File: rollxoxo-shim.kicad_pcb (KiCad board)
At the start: 4 copper layers, 70 parts, among them J1 USB_C_Receptacle_USB2.0_14P, J2 Conn_01x02, J3 Conn_01x10, J4 Conn_01x01, J5 Conn_01x10, J6 Conn_01x03, J7 Conn_01x01, SW1 SW_Push, SW2 SW_Push, U1 SN74LV1T125DBV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

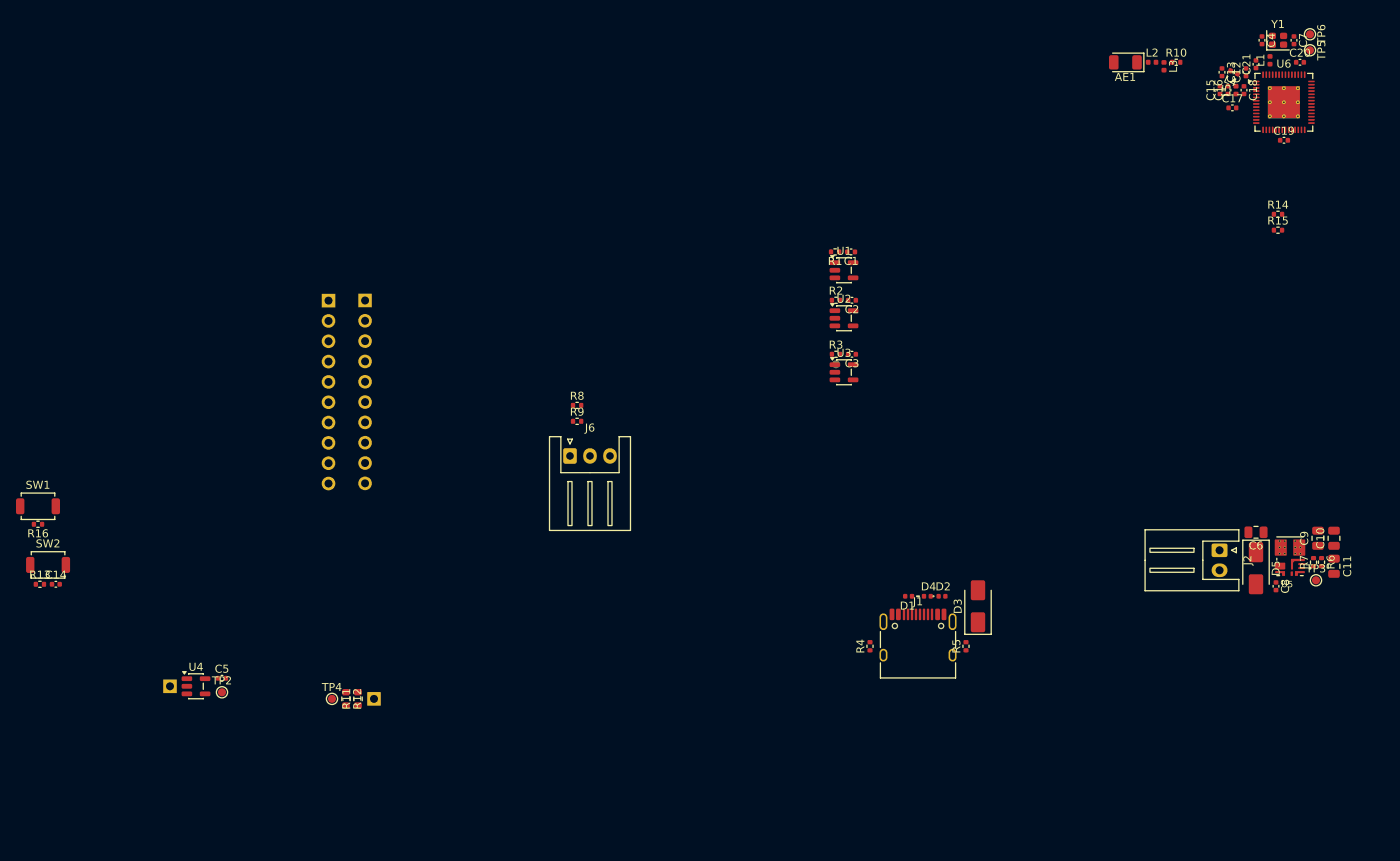
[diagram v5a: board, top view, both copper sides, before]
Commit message: pcb: refine layout
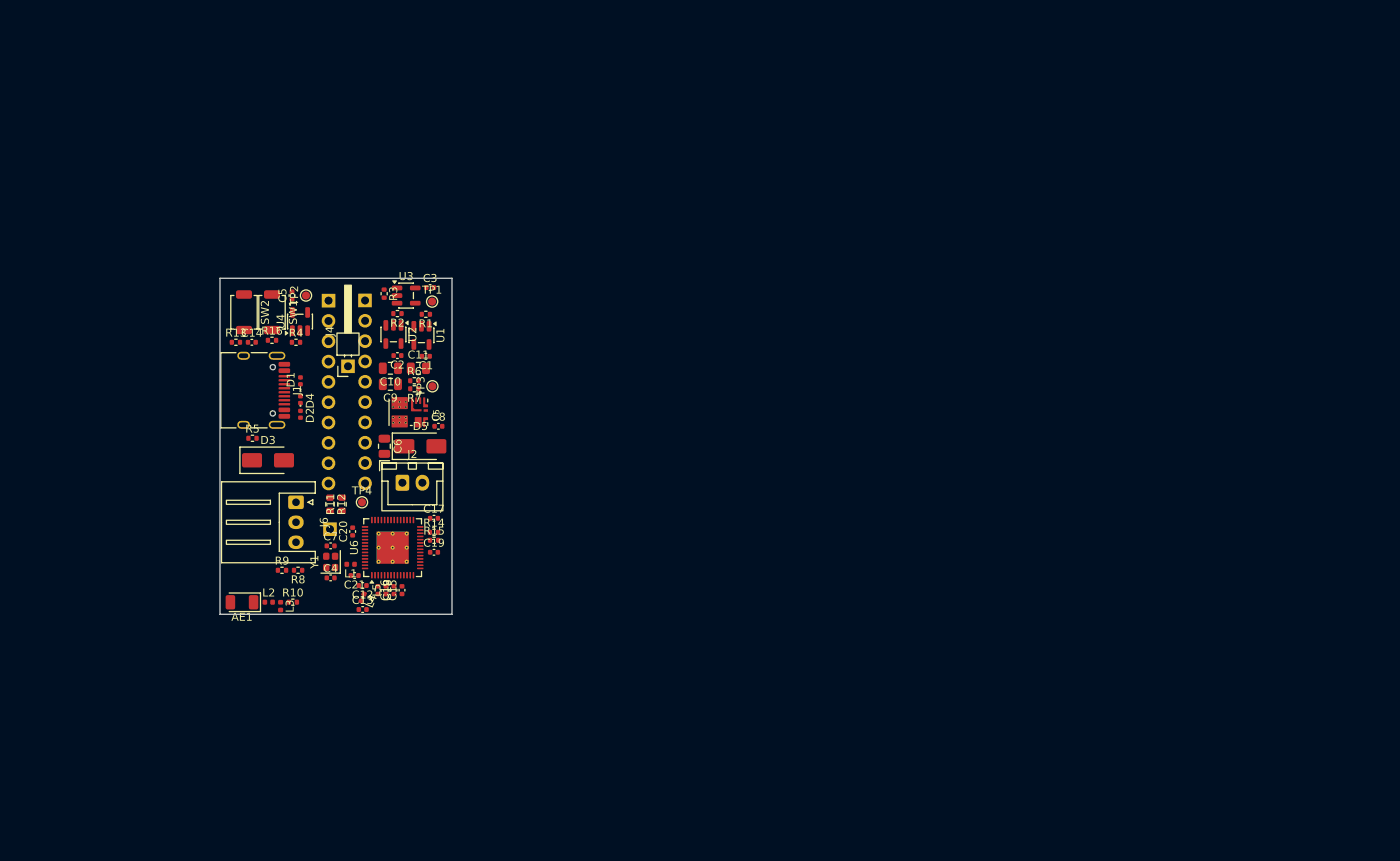
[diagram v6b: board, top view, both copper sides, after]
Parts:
- removed TP5, TP6: TestPoint, TestPoint:TestPoint_Pad_D1.0mm
- J2: footprint Connector_JST:JST_XH_S2B-XH-A_1x02_P2.50mm_Horizontal -> Connector_JST:JST_XH_B2B-XH-A_1x02_P2.50mm_Vertical
- J4, TP1: moved to F.Cu
- moved C7 136.0 mm to (67.8, 151.4), turned to 0 degrees
- moved Y1 135.2 mm to (67.8, 153.4), turned to 90 degrees
- moved C4 134.4 mm to (67.8, 155.4), turned to 0 degrees
- moved C20 132.2 mm to (70.6, 149.7), turned to 90 degrees
- moved L1 131.1 mm to (70.3, 153.8), turned to 180 degrees
- moved C21 129.5 mm to (70.8, 155.2), turned to 180 degrees
- moved AE1 129.4 mm to (56.8, 158.5)
- moved L3 129.4 mm to (61.6, 159.0)
- moved R10 129.4 mm to (63.1, 158.5)
- moved L2 129.4 mm to (60.1, 158.5)
- moved C12 127.7 mm to (71.8, 156.4), turned to 180 degrees
- moved L4 127.2 mm to (71.8, 157.9), turned to -112.5 degrees
- moved C13 126.7 mm to (71.8, 159.4), turned to 0 degrees
- moved C18 125.0 mm to (73.8, 157.0)
- moved U6 124.5 mm to (75.6, 151.7), turned to 90 degrees
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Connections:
- J1 pad SH: (no net) -> GND
- U6 pad 49: Net-(U6-U0TXD/PROG/GPIO43) -> unconnected-(U6-U0TXD/PROG/GPIO43-Pad49)
- U6 pad 50: Net-(U6-U0RXD/PROG/GPIO44) -> unconnected-(U6-U0RXD/PROG/GPIO44-Pad50)
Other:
- board outline added: 29 x 42 mm

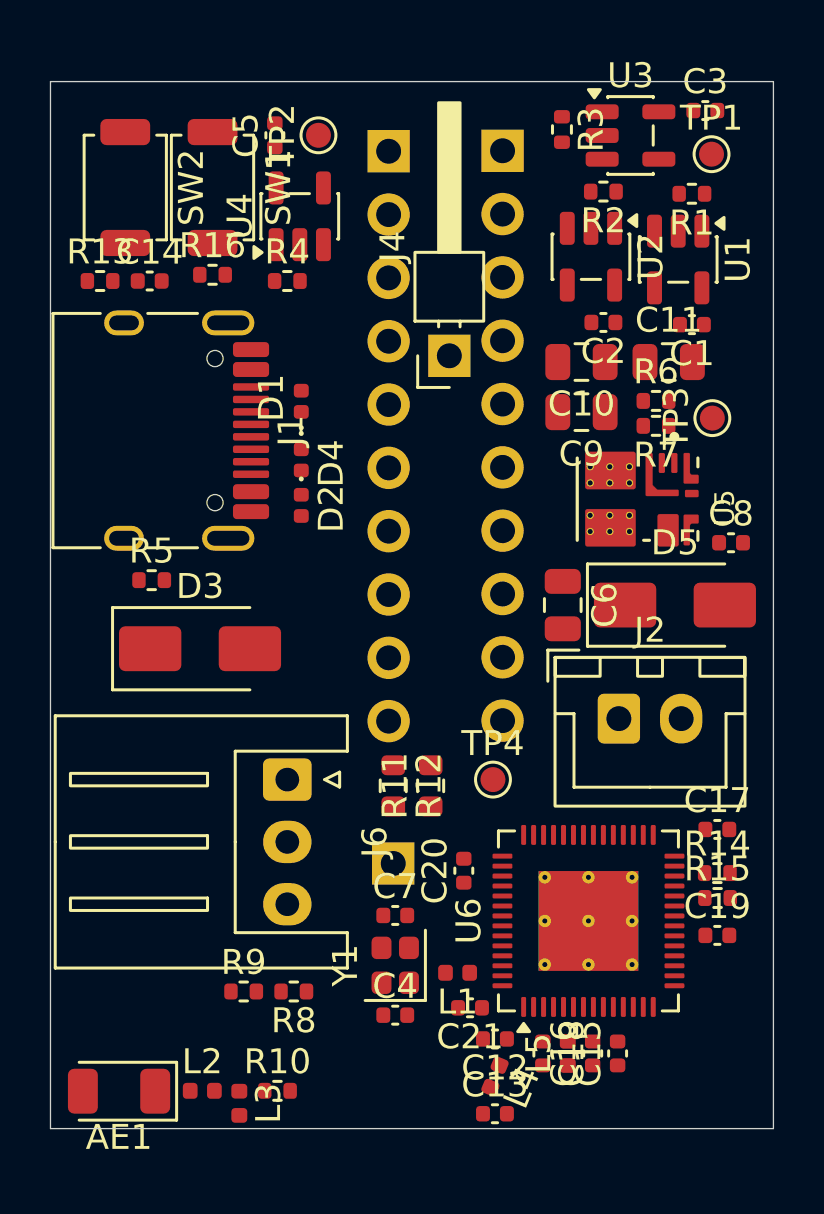
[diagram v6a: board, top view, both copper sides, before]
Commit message: pcb: add board outline
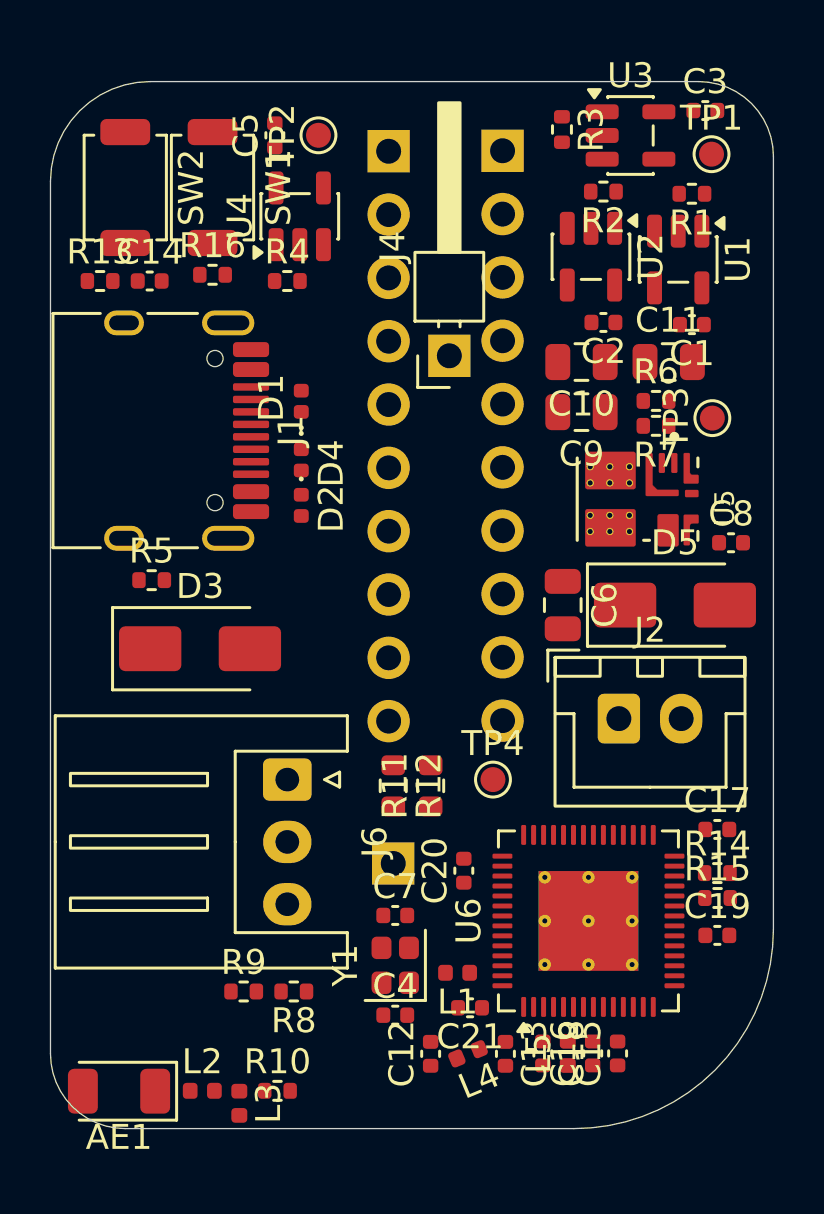
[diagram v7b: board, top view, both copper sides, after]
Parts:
- moved C12 2.65 mm to (69.2, 157.0), turned to 90 degrees
- moved C13 2.44 mm to (72.2, 157.0), turned to -90 degrees
- moved L4 1.41 mm to (70.8, 157.0), turned to -157.5 degrees
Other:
- outline, holes or cut-outs redrawn
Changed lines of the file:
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@@
 	(footprint "Capacitor_SMD:C_0402_1005Metric"
 		(layer "F.Cu")
-		(at 71.83 159.405)
+		(at 72.25 157 -90)
 		(descr "Capacitor SMD 0402 (1005 Metric), square (rectangular) end terminal, IPC-7351 nominal, (Body size source: IPC-SM-782 page 76, https://www.pcb-3d.com/wordpress/wp-content/uploads/ipc-sm-782a_amendment_1_and_2.pdf)")
 		(tags "capacitor")
 		(property "Reference" "C13"
-			(at 0 -1.16 0)
+			(at 0 -1.16 90)
 			(layer "F.SilkS")
 			(effects
@@
 		)
 		(property "Value" "1p2"
-			(at 0 1.16 0)
+			(at 0 1.16 90)
 			(layer "F.Fab")
 			(effects
@@
 		)
 		(property "Datasheet" ""
-			(at 0 0 0)
+			(at 0 0 90)
 			(layer "F.Fab")
 			(hide yes)
@@
 		)
 		(property "Description" "Unpolarized capacitor"
-			(at 0 0 0)
+			(at 0 0 90)
 			(layer "F.Fab")
 			(hide yes)
@@
 		)
 		(property "KiLib_Generator" "SMD_2terminal_chip_molded"
-			(at 0 0 0)
+			(at 0 0 90)
 			(layer "F.SilkS")
 			(hide yes)
@@
 		)
 		(property "Manufacturer" "Murata"
-			(at 0 0 0)
+			(at 0 0 270)
 			(unlocked yes)
 			(layer "F.Fab")
@@
 		)
 		(property "Manufacturer Part Number" "GJM1555C1H1R2WB01D"
-			(at 0 0 0)
+			(at 0 0 270)
 			(unlocked yes)
 			(layer "F.Fab")
@@
 		)
 		(property "Basic" "X"
-			(at 0 0 0)
+			(at 0 0 270)
 			(unlocked yes)
 			(layer "F.Fab")
@@
 		)
 		(property "JLCPCB Part #" "C76899"
-			(at 0 0 0)
+			(at 0 0 270)
 			(unlocked yes)
 			(layer "F.Fab")
@@
 		(duplicate_pad_numbers_are_jumpers no)
 		(fp_line
-			(start -0.107836 -0.36)
-			(end 0.107836 -0.36)
+			(start -0.107836 0.36)
+			(end 0.107836 0.36)
 			(stroke
 				(width 0.12)
@@
 		)
 		(fp_line
-			(start -0.107836 0.36)
-			(end 0.107836 0.36)
+			(start -0.107836 -0.36)
+			(end 0.107836 -0.36)
 			(stroke
 				(width 0.12)
@@
 		)
 		(fp_text user "${REFERENCE}"
-			(at 0 0 0)
+			(at 0 0 90)
 			(layer "F.Fab")
 			(effects
@@
 		)
 		(pad "1" smd roundrect
-			(at -0.48 0)
+			(at -0.48 0 270)
 			(size 0.56 0.62)
 			(layers "F.Cu" "F.Mask" "F.Paste")
@@
 		)
 		(pad "2" smd roundrect
-			(at 0.48 0)
+			(at 0.48 0 270)
 			(size 0.56 0.62)
 			(layers "F.Cu" "F.Mask" "F.Paste")
@@
 	(footprint "Capacitor_SMD:C_0402_1005Metric"
 		(layer "F.Cu")
-		(at 71.83 156.405 180)
+		(at 69.25 157 90)
 		(descr "Capacitor SMD 0402 (1005 Metric), square (rectangular) end terminal, IPC-7351 nominal, (Body size source: IPC-SM-782 page 76, https://www.pcb-3d.com/wordpress/wp-content/uploads/ipc-sm-782a_amendment_1_and_2.pdf)")
 		(tags "capacitor")
 		(property "Reference" "C12"
-			(at 0 -1.16 0)
+			(at 0 -1.16 90)
 			(layer "F.SilkS")
 			(effects
@@
 		)
 		(property "Value" "1p2"
-			(at 0 1.16 0)
+			(at 0 1.16 90)
 			(layer "F.Fab")
 			(effects
@@
 		)
 		(property "Datasheet" ""
-			(at 0 0 0)
+			(at 0 0 90)
 			(layer "F.Fab")
 			(hide yes)
@@
 		)
 		(property "Description" "Unpolarized capacitor"
-			(at 0 0 0)
+			(at 0 0 90)
 			(layer "F.Fab")
 			(hide yes)
@@
 		)
 		(property "KiLib_Generator" "SMD_2terminal_chip_molded"
-			(at 0 0 0)
+			(at 0 0 90)
 			(layer "F.SilkS")
 			(hide yes)
@@
 		)
 		(property "Manufacturer" "Murata"
-			(at 0 0 180)
+			(at 0 0 90)
 			(unlocked yes)
 			(layer "F.Fab")
@@
 		)
 		(property "Manufacturer Part Number" "GJM1555C1H1R2WB01D"
-			(at 0 0 180)
+			(at 0 0 90)
 			(unlocked yes)
 			(layer "F.Fab")
@@
 		)
 		(property "Basic" "X"
-			(at 0 0 180)
+			(at 0 0 90)
 			(unlocked yes)
 			(layer "F.Fab")
@@
 		)
 		(property "JLCPCB Part #" "C76899"
-			(at 0 0 180)
+			(at 0 0 90)
 			(unlocked yes)
 			(layer "F.Fab")
@@
 		(duplicate_pad_numbers_are_jumpers no)
 		(fp_line
-			(start -0.107836 0.36)
-			(end 0.107836 0.36)
+			(start -0.107836 -0.36)
+			(end 0.107836 -0.36)
 			(stroke
 				(width 0.12)
@@
 		)
 		(fp_line
-			(start -0.107836 -0.36)
-			(end 0.107836 -0.36)
+			(start -0.107836 0.36)
+			(end 0.107836 0.36)
 			(stroke
 				(width 0.12)
@@
 		)
 		(fp_text user "${REFERENCE}"
-			(at 0 0 0)
+			(at 0 0 90)
 			(layer "F.Fab")
 			(effects
@@
 		)
 		(pad "1" smd roundrect
-			(at -0.48 0 180)
+			(at -0.48 0 90)
 			(size 0.56 0.62)
 			(layers "F.Cu" "F.Mask" "F.Paste")
@@
 		)
 		(pad "2" smd roundrect
-			(at 0.48 0 180)
+			(at 0.48 0 90)
 			(size 0.56 0.62)
 			(layers "F.Cu" "F.Mask" "F.Paste")
@@
 	(footprint "Inductor_SMD:L_0402_1005Metric"
 		(layer "F.Cu")
-		(at 71.83 157.905 -112.5)
+		(at 70.75 157 -157.5)
 		(descr "Inductor SMD 0402 (1005 Metric), square (rectangular) end terminal, IPC-7351 nominal, (Body size source: http://www.tortai-tech.com/upload/download/2011102023233369053.pdf)")
 		(tags "inductor")
 		(property "Reference" "L4"
-			(at 0 -1.17 67.5)
+			(at 0 -1.17 22.5)
 			(layer "F.SilkS")
 			(effects
@@
 		)
 		(property "Value" "2n7"
-			(at 0 1.17 67.5)
+			(at 0 1.17 22.5)
 			(layer "F.Fab")
 			(effects
@@
 		)
 		(property "Datasheet" ""
-			(at 0 0 67.5)
+			(at 0 0 22.5)
 			(layer "F.Fab")
 			(hide yes)
@@
 		)
 		(property "Description" "Inductor"
-			(at 0 0 67.5)
+			(at 0 0 22.5)
 			(layer "F.Fab")
 			(hide yes)
@@
 		)
 		(property "KiLib_Generator" "SMD_2terminal_chip_molded"
-			(at 0 0 67.5)
+			(at 0 0 22.5)
 			(layer "F.SilkS")
 			(hide yes)
@@
 		)
 		(property "Manufacturer" "Murata"
-			(at 0 0 247.5)
+			(at 0 0 202.5)
 			(unlocked yes)
 			(layer "F.Fab")
@@
 		)
 		(property "Manufacturer Part Number" "LQG15HS2N7S02D"
-			(at 0 0 247.5)
+			(at 0 0 202.5)
 			(unlocked yes)
 			(layer "F.Fab")
@@
 		)
 		(property "Basic" "X"
-			(at 0 0 247.5)
+			(at 0 0 202.5)
 			(unlocked yes)
 			(layer "F.Fab")
@@
 		)
 		(property "JLCPCB Part #" "C77108"
-			(at 0 0 247.5)
+			(at 0 0 202.5)
 			(unlocked yes)
 			(layer "F.Fab")
@@
 		)
 		(fp_text user "${REFERENCE}"
-			(at 0 0 67.5)
+			(at 0 0 22.5)
 			(layer "F.Fab")
 			(effects
@@
 		)
 		(pad "1" smd roundrect
-			(at -0.485 0.000001 247.5)
+			(at -0.485 0.000001 202.5)
 			(size 0.59 0.64)
 			(layers "F.Cu" "F.Mask" "F.Paste")
@@
 		)
 		(pad "2" smd roundrect
-			(at 0.485 -0.000001 247.5)
+			(at 0.485 -0.000001 202.5)
 			(size 0.59 0.64)
 			(layers "F.Cu" "F.Mask" "F.Paste")
@@
 		)
 	)
-	(gr_rect
-		(start 54 118)
-		(end 83 160)
+	(gr_arc
+		(start 54 122)
+		(mid 55.171573 119.171573)
+		(end 58 118)
+		(stroke
+			(width 0.05)
+			(type default)
+		)
+		(layer "Edge.Cuts")
+	)
+	(gr_line
+		(start 54 157)
+		(end 54 122)
+		(stroke
+			(width 0.05)
+			(type default)
+		)
+		(layer "Edge.Cuts")
+	)
+	(gr_arc
+		(start 57 160)
+		(mid 54.87868 159.12132)
+		(end 54 157)
+		(stroke
+			(width 0.05)
+			(type default)
+		)
+		(layer "Edge.Cuts")
+	)
+	(gr_line
+		(start 58 118)
+		(end 80 118)
+		(stroke
+			(width 0.05)
+			(type default)
+		)
+		(layer "Edge.Cuts")
+	)
+	(gr_line
+		(start 75 160)
+		(end 57 160)
+		(stroke
+			(width 0.05)
+			(type default)
+		)
+		(layer "Edge.Cuts")
+	)
+	(gr_arc
+		(start 80 118)
+		(mid 82.12132 118.87868)
+		(end 83 121)
+		(stroke
+			(width 0.05)
+			(type default)
+		)
+		(layer "Edge.Cuts")
+	)
+	(gr_line
+		(start 83 121)
+		(end 83 152)
+		(stroke
+			(width 0.05)
+			(type default)
+		)
+		(layer "Edge.Cuts")
+	)
+	(gr_arc
+		(start 83 152)
+		(mid 80.656854 157.656854)
+		(end 75 160)
 		(stroke
 			(width 0.05)
 			(type default)
 		)
-		(fill no)
 		(layer "Edge.Cuts")
 	)

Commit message: pcb: add gnd planes
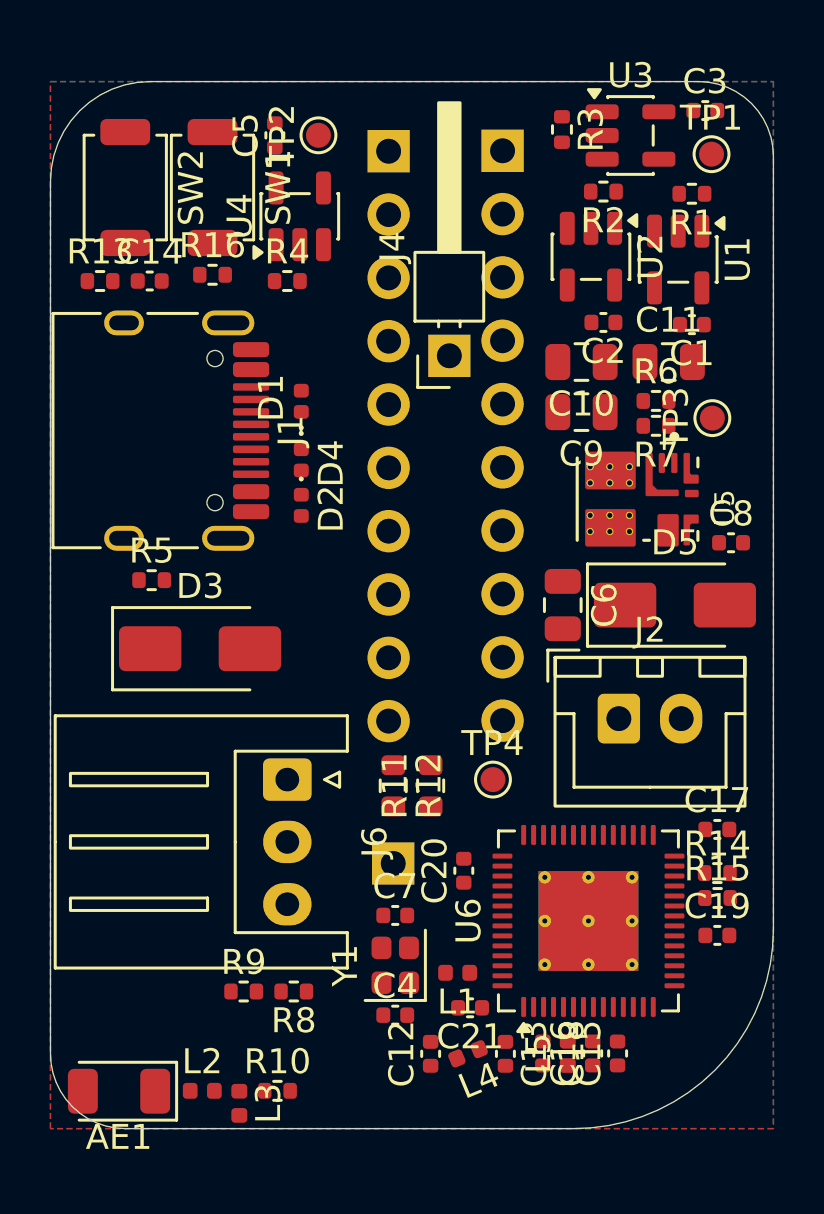
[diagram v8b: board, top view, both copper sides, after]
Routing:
- added copper zone on B.Cu, net GND
- added copper zone on F.Cu, net GND
- added copper zone on In1.Cu, net GND
- added copper zone on In2.Cu, net GND
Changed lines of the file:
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@@
 		(layer "Edge.Cuts")
+	)
+	(zone
+		(net "GND")
+		(layers "F.Cu" "B.Cu" "In1.Cu" "In2.Cu")
+		(hatch edge 0.5)
+		(connect_pads
+			(clearance 0.2)
+		)
+		(min_thickness 0.15)
+		(fill yes
+			(thermal_gap 0.35)
+			(thermal_bridge_width 0.35)
+			(island_removal_mode 0)
+		)
+		(polygon
+			(pts
+				(xy 54 118) (xy 83 118) (xy 83 160) (xy 54 160)
+			)
+		)
 	)
 	(embedded_fonts no)
